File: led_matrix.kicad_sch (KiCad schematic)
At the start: 160 parts, among them Q1 BSS84, Q10 BSS84, Q11 2N7002, Q12 2N7002, Q13 2N7002, Q14 2N7002, Q15 2N7002, Q16 2N7002, Q17 2N7002, Q18 2N7002, Q19 2N7002, Q2 BSS84, Q20 2N7002, Q3 BSS84, Q4 BSS84, Q5 BSS84, Q6 BSS84, Q7 BSS84, Q8 BSS84, Q9 BSS84

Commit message: improved design of the matrix
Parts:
- added R12, R15, R18, R21, R24, R27, R30, R33, R6, R9: 47, Resistor_SMD:R_0603_1608Metric, symbol Device:R
- renumbered R8 to R10, R9 to R11, R10 to R13, R11 to R14, R14 to R16, R15 to R17, R16 to R19, R17 to R20, R18 to R22, R19 to R23, R20 to R25, R21 to R26, R22 to R28, R23 to R29, R24 to R31, R25 to R32, R26 to R34, R27 to R35, R13 to R36, R28 to R37, R30 to R38, R31 to R39, R34 to R40, R35 to R41, R38 to R42, R39 to R43, R42 to R44, R43 to R45, R12 to R46, R29 to R47, R32 to R48, R33 to R49, R36 to R50, R37 to R51, R40 to R52, R41 to R53, R44 to R54, R45 to R55, R2 to R7, R3 to R8
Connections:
- removed net +5V: Q1.2 (S), Q10.2 (S), Q2.2 (S), Q3.2 (S), Q4.2 (S), Q5.2 (S), Q6.2 (S), Q7.2 (S), Q8.2 (S), Q9.2 (S), R11.2, R14.2, R17.2, R20.2, R23.2, R26.2, R29.2, R32.2, R35.2, R8.2
- new net: Q7.2 (S), R24.2, R26.2
- new net: Q1.2 (S), R6.2, R8.2
- new net: Q8.2 (S), R27.2, R29.2
- new net: Q10.2 (S), R33.2, R35.2
- new net: Q4.2 (S), R15.2, R17.2
- new net: Q2.2 (S), R11.2, R9.2
- new net: Q6.2 (S), R21.2, R23.2
- new net: Q3.2 (S), R12.2, R14.2
- new net: Q5.2 (S), R18.2, R20.2
- new net: Q9.2 (S), R30.2, R32.2
- new net +3.3V: R12.1, R15.1, R18.1, R21.1, R24.1, R27.1, R30.1, R33.1, R6.1, R9.1
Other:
- moved on the sheet: R10, R13, R16, R19, R22, R25, R28, R31, R34, R7

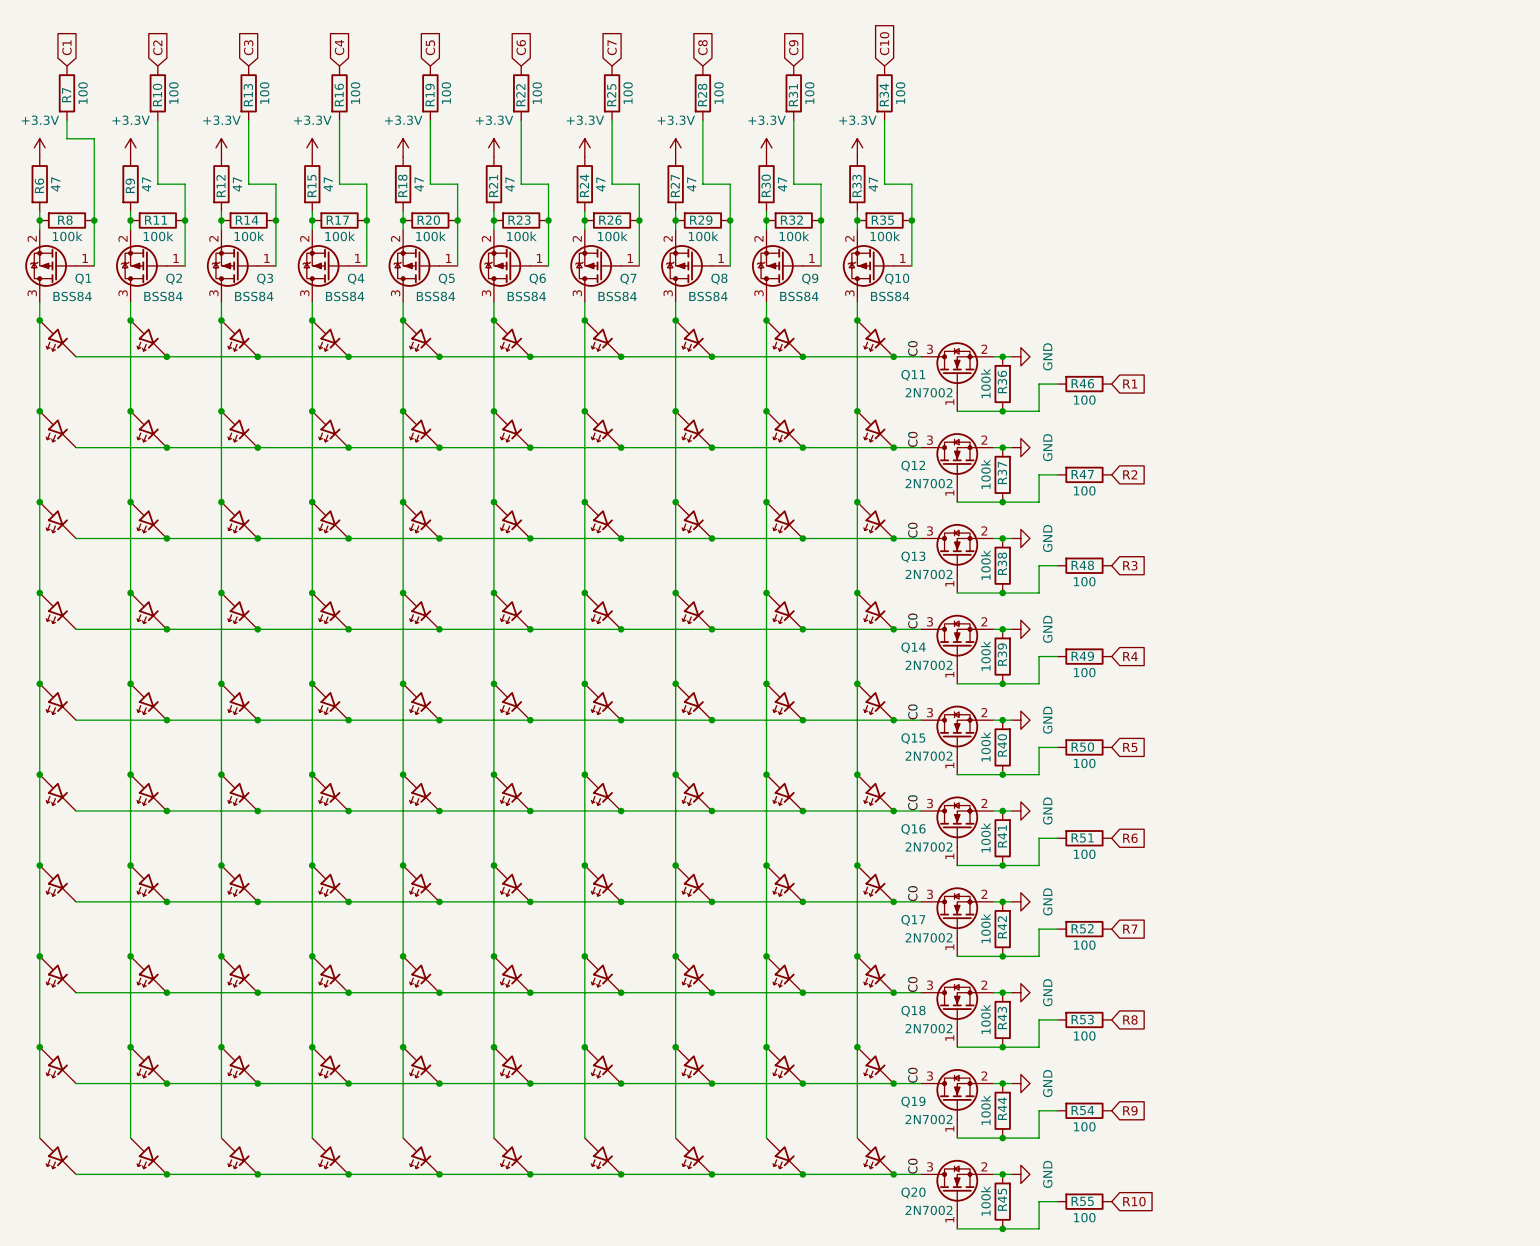
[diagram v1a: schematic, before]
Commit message: improved design and starting to layout the components
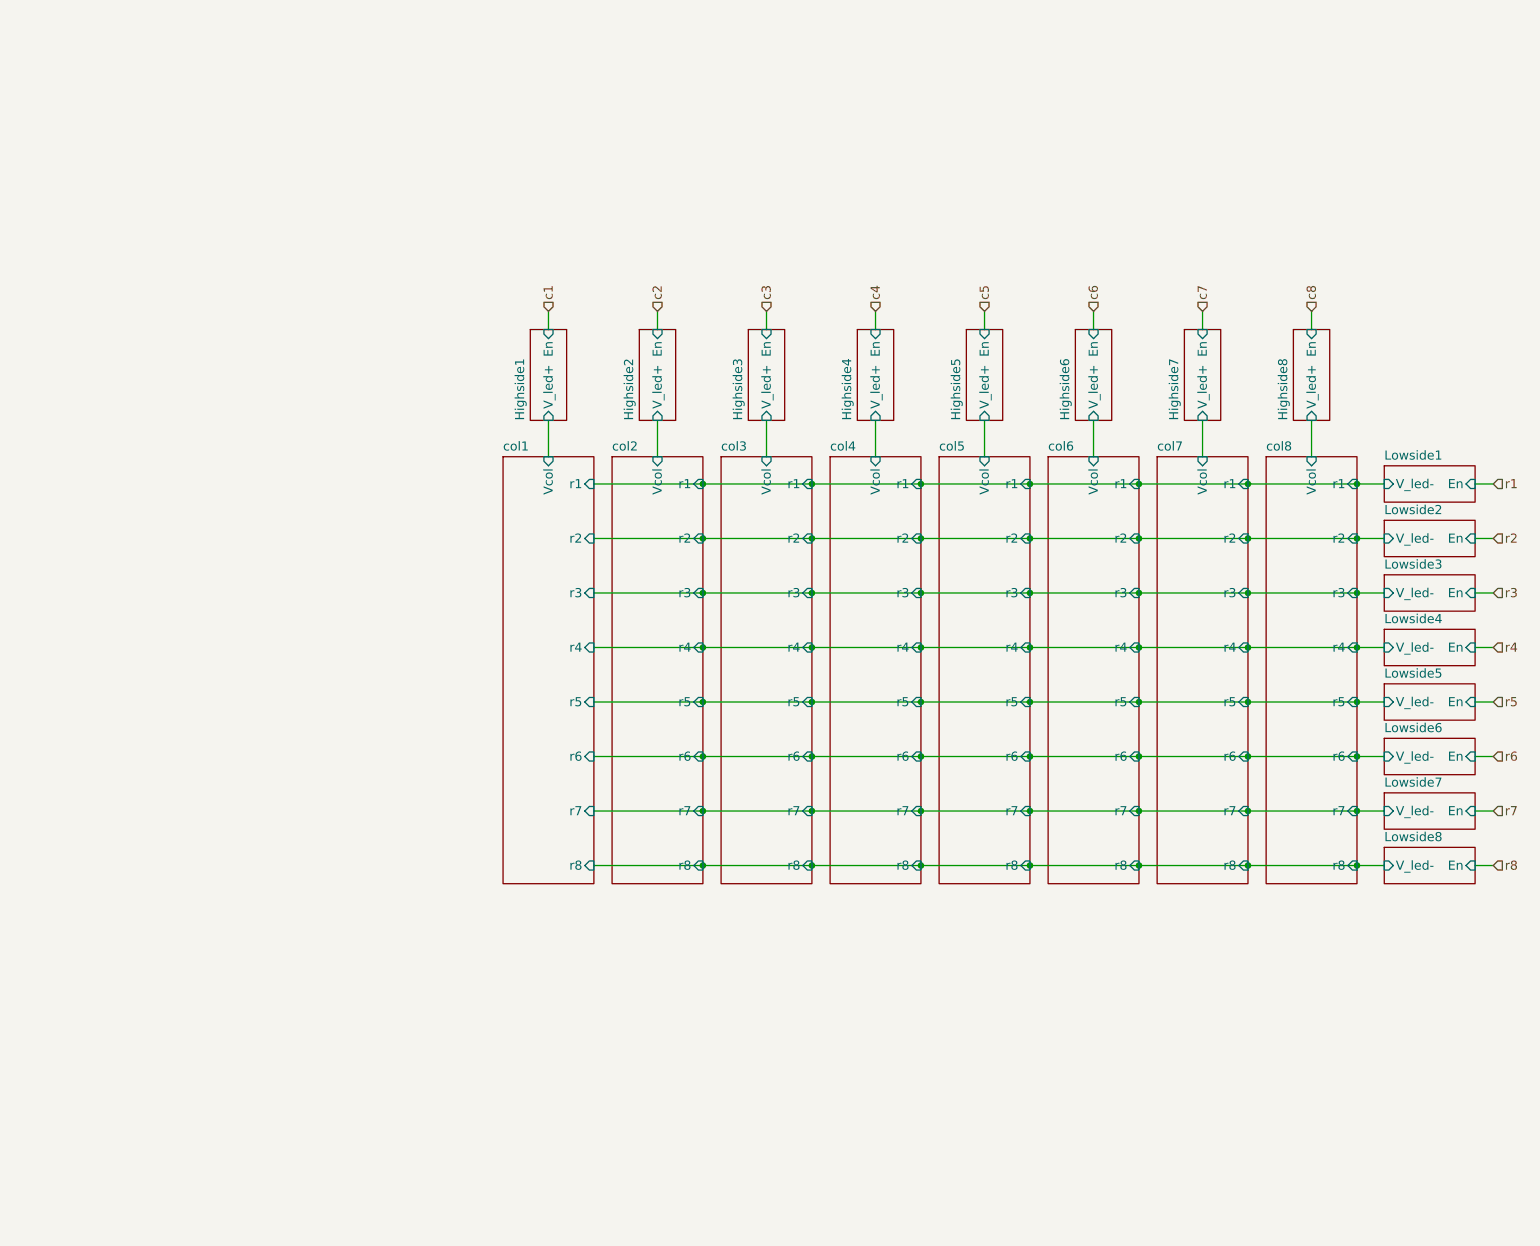
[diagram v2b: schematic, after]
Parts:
- removed D1, D10, D100, D11, D12, D13, D14, D15, D16, D17, D18, D19, D2, D20, D21, D22, D23, D24, D25, D26, D27, D28, D29, D3, D30, D31, D32, D33, D34, D35, D36, D37, D38, D39, D4, D40, D41, D42, D43, D44, D45, D46, D47, D48, D49, D5, D50, D51, D52, D53, D54, D55, D56, D57, D58, D59, D6, D60, D61, D62, D63, D64, D65, D66, D67, D68, D69, D7, D70, D71, D72, D73, D74, D75, D76, D77, D78, D79, D8, D80, D81, D82, D83, D84, D85, D86, D87, D88, D89, D9, D90, D91, D92, D93, D94, D95, D96, D97, D98, D99: LED_45deg, LED_SMD:LED_0603_1608Metric, symbol Device:LED_45deg
- removed Q1, Q10, Q2, Q3, Q4, Q5, Q6, Q7, Q8, Q9: BSS84, Package_TO_SOT_SMD:SOT-23, symbol Transistor_FET:BSS84
- removed Q11, Q12, Q13, Q14, Q15, Q16, Q17, Q18, Q19, Q20: 2N7002, Package_TO_SOT_SMD:SOT-23, symbol Transistor_FET:2N7002
- removed R10, R13, R16, R19, R22, R25, R28, R31, R34, R46, R47, R48, R49, R50, R51, R52, R53, R54, R55, R7: 100, Resistor_SMD:R_0603_1608Metric, symbol Device:R
- removed R11, R14, R17, R20, R23, R26, R29, R32, R35, R36, R37, R38, R39, R40, R41, R42, R43, R44, R45, R8: 100k, Resistor_SMD:R_0603_1608Metric, symbol Device:R
- removed R12, R15, R18, R21, R24, R27, R30, R33, R6, R9: 47, Resistor_SMD:R_0603_1608Metric, symbol Device:R
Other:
- added sheet Highside1 (highside_driver.kicad_sch)
- added sheet Highside2 (highside_driver.kicad_sch)
- added sheet Highside3 (highside_driver.kicad_sch)
- added sheet Highside4 (highside_driver.kicad_sch)
- added sheet Highside5 (highside_driver.kicad_sch)
- added sheet Highside6 (highside_driver.kicad_sch)
- added sheet Highside7 (highside_driver.kicad_sch)
- added sheet Highside8 (highside_driver.kicad_sch)
- added sheet Lowside1 (lowside_driver.kicad_sch)
- added sheet Lowside2 (lowside_driver.kicad_sch)
- added sheet Lowside3 (lowside_driver.kicad_sch)
- added sheet Lowside4 (lowside_driver.kicad_sch)
- added sheet Lowside5 (lowside_driver.kicad_sch)
- added sheet Lowside6 (lowside_driver.kicad_sch)
- added sheet Lowside7 (lowside_driver.kicad_sch)
- added sheet Lowside8 (lowside_driver.kicad_sch)
- added sheet col1 (led_col.kicad_sch)
- added sheet col2 (led_col.kicad_sch)
- added sheet col3 (led_col.kicad_sch)
- added sheet col4 (led_col.kicad_sch)
- added sheet col5 (led_col.kicad_sch)
- added sheet col6 (led_col.kicad_sch)
- added sheet col7 (led_col.kicad_sch)
- added sheet col8 (led_col.kicad_sch)
